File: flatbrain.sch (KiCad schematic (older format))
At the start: 107 parts, among them J1 OLED, SW41 Rotary_Encoder_Switch, SW42 Rotary_Encoder_Switch, U1 Elite-C

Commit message: wip: switches placed, matrix change
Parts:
- removed D1, D12, D13, D24, D25, D36, D37, D46: D_Small, Keebio-Parts:Diode-Hybrid-Back, symbol Device:D_Small
- removed JP1, JP2, JP3: Jumper_NO_Small, Jumper:SolderJumper-2_P1.3mm_Open_Pad1.0x1.5mm, symbol Device:Jumper_NO_Small
- removed MX1, MX12, MX13, MX24, MX25, MX36, MX37, MX46: MX-NoLED, parts:mxchoc_1u, symbol MX_Alps_Hybrid:MX-NoLED
- D1: renamed from D2; footprint Keebio-Parts:Diode-Hybrid-Back -> Keebio-Parts:Diode-dual
- D10: renamed from D11; footprint Keebio-Parts:Diode-Hybrid-Back -> Keebio-Parts:Diode-dual
- D11: renamed from D14; footprint Keebio-Parts:Diode-Hybrid-Back -> Keebio-Parts:Diode-dual
- D12: renamed from D15; footprint Keebio-Parts:Diode-Hybrid-Back -> Keebio-Parts:Diode-dual
- D13: renamed from D16; footprint Keebio-Parts:Diode-Hybrid-Back -> Keebio-Parts:Diode-dual
- D14: renamed from D17; footprint Keebio-Parts:Diode-Hybrid-Back -> Keebio-Parts:Diode-dual
- D15: renamed from D18; footprint Keebio-Parts:Diode-Hybrid-Back -> Keebio-Parts:Diode-dual
- D16: renamed from D19; footprint Keebio-Parts:Diode-Hybrid-Back -> Keebio-Parts:Diode-dual
- D17: renamed from D20; footprint Keebio-Parts:Diode-Hybrid-Back -> Keebio-Parts:Diode-dual
- D18: renamed from D21; footprint Keebio-Parts:Diode-Hybrid-Back -> Keebio-Parts:Diode-dual
- D19: renamed from D22; footprint Keebio-Parts:Diode-Hybrid-Back -> Keebio-Parts:Diode-dual
- D2: renamed from D3; footprint Keebio-Parts:Diode-Hybrid-Back -> Keebio-Parts:Diode-dual
- D20: renamed from D23; footprint Keebio-Parts:Diode-Hybrid-Back -> Keebio-Parts:Diode-dual
- D21: renamed from D26; footprint Keebio-Parts:Diode-Hybrid-Back -> Keebio-Parts:Diode-dual
- D22: renamed from D27; footprint Keebio-Parts:Diode-Hybrid-Back -> Keebio-Parts:Diode-dual
- D23: renamed from D28; footprint Keebio-Parts:Diode-Hybrid-Back -> Keebio-Parts:Diode-dual
- D24: renamed from D29; footprint Keebio-Parts:Diode-Hybrid-Back -> Keebio-Parts:Diode-dual
- D25: renamed from D30; footprint Keebio-Parts:Diode-Hybrid-Back -> Keebio-Parts:Diode-dual
- D26: renamed from D31; footprint Keebio-Parts:Diode-Hybrid-Back -> Keebio-Parts:Diode-dual
- D27: renamed from D32; footprint Keebio-Parts:Diode-Hybrid-Back -> Keebio-Parts:Diode-dual
- D28: renamed from D33; footprint Keebio-Parts:Diode-Hybrid-Back -> Keebio-Parts:Diode-dual
- D29: renamed from D34; footprint Keebio-Parts:Diode-Hybrid-Back -> Keebio-Parts:Diode-dual
- D3: renamed from D4; footprint Keebio-Parts:Diode-Hybrid-Back -> Keebio-Parts:Diode-dual
- D30: renamed from D35; footprint Keebio-Parts:Diode-Hybrid-Back -> Keebio-Parts:Diode-dual
- D32: renamed from D38; footprint Keebio-Parts:Diode-Hybrid-Back -> Keebio-Parts:Diode-dual
- D33: renamed from D39; footprint Keebio-Parts:Diode-Hybrid-Back -> Keebio-Parts:Diode-dual
- D34: renamed from D40; footprint Keebio-Parts:Diode-Hybrid-Back -> Keebio-Parts:Diode-dual
- D35: renamed from D41; footprint Keebio-Parts:Diode-Hybrid-Back -> Keebio-Parts:Diode-dual
- D36: renamed from D42; footprint Keebio-Parts:Diode-Hybrid-Back -> Keebio-Parts:Diode-dual
- D37: renamed from D43; footprint Keebio-Parts:Diode-Hybrid-Back -> Keebio-Parts:Diode-dual
- D38: renamed from D44; footprint Keebio-Parts:Diode-Hybrid-Back -> Keebio-Parts:Diode-dual
- D39: renamed from D45; footprint Keebio-Parts:Diode-Hybrid-Back -> Keebio-Parts:Diode-dual
- D4: renamed from D5; footprint Keebio-Parts:Diode-Hybrid-Back -> Keebio-Parts:Diode-dual
- D5: renamed from D6; footprint Keebio-Parts:Diode-Hybrid-Back -> Keebio-Parts:Diode-dual
- D6: renamed from D7; footprint Keebio-Parts:Diode-Hybrid-Back -> Keebio-Parts:Diode-dual
- D7: renamed from D8; footprint Keebio-Parts:Diode-Hybrid-Back -> Keebio-Parts:Diode-dual
- D8: renamed from D9; footprint Keebio-Parts:Diode-Hybrid-Back -> Keebio-Parts:Diode-dual
- D9: renamed from D10; footprint Keebio-Parts:Diode-Hybrid-Back -> Keebio-Parts:Diode-dual
- MX1: renamed from MX2; footprint parts:mxchoc_1u -> parts:mix_1u; symbol MX_Alps_Hybrid:MX-NoLED -> flatbrain:MX_Alps_Hybrid_MX-NoLED
- MX10: renamed from MX11; footprint parts:mxchoc_1u -> parts:mix_1u; symbol MX_Alps_Hybrid:MX-NoLED -> flatbrain:MX_Alps_Hybrid_MX-NoLED
- MX11: renamed from MX14; footprint parts:mxchoc_1u -> parts:mix_1u; symbol MX_Alps_Hybrid:MX-NoLED -> flatbrain:MX_Alps_Hybrid_MX-NoLED
- MX12: renamed from MX15; footprint parts:mxchoc_1u -> parts:mix_1u; symbol MX_Alps_Hybrid:MX-NoLED -> flatbrain:MX_Alps_Hybrid_MX-NoLED
- MX13: renamed from MX16; footprint parts:mxchoc_1u -> parts:mix_1u; symbol MX_Alps_Hybrid:MX-NoLED -> flatbrain:MX_Alps_Hybrid_MX-NoLED
- MX14: renamed from MX17; footprint parts:mxchoc_1u -> parts:mix_1u; symbol MX_Alps_Hybrid:MX-NoLED -> flatbrain:MX_Alps_Hybrid_MX-NoLED
- MX15: renamed from MX18; footprint parts:mxchoc_1u -> parts:mix_1u; symbol MX_Alps_Hybrid:MX-NoLED -> flatbrain:MX_Alps_Hybrid_MX-NoLED
- MX16: renamed from MX19; footprint parts:mxchoc_1u -> parts:mix_1u; symbol MX_Alps_Hybrid:MX-NoLED -> flatbrain:MX_Alps_Hybrid_MX-NoLED
- MX17: renamed from MX20; footprint parts:mxchoc_1u -> parts:mix_1u; symbol MX_Alps_Hybrid:MX-NoLED -> flatbrain:MX_Alps_Hybrid_MX-NoLED
- MX18: renamed from MX21; footprint parts:mxchoc_1u -> parts:mix_1u; symbol MX_Alps_Hybrid:MX-NoLED -> flatbrain:MX_Alps_Hybrid_MX-NoLED
- MX19: renamed from MX22; footprint parts:mxchoc_1u -> parts:mix_1u; symbol MX_Alps_Hybrid:MX-NoLED -> flatbrain:MX_Alps_Hybrid_MX-NoLED
- MX2: renamed from MX3; footprint parts:mxchoc_1u -> parts:mix_1u; symbol MX_Alps_Hybrid:MX-NoLED -> flatbrain:MX_Alps_Hybrid_MX-NoLED
- MX20: renamed from MX23; footprint parts:mxchoc_1u -> parts:mix_1u; symbol MX_Alps_Hybrid:MX-NoLED -> flatbrain:MX_Alps_Hybrid_MX-NoLED
- MX21: renamed from MX26; footprint parts:mxchoc_1u -> parts:mix_1u; symbol MX_Alps_Hybrid:MX-NoLED -> flatbrain:MX_Alps_Hybrid_MX-NoLED
- MX22: renamed from MX27; footprint parts:mxchoc_1u -> parts:mix_1u; symbol MX_Alps_Hybrid:MX-NoLED -> flatbrain:MX_Alps_Hybrid_MX-NoLED
- MX23: renamed from MX28; footprint parts:mxchoc_1u -> parts:mix_1u; symbol MX_Alps_Hybrid:MX-NoLED -> flatbrain:MX_Alps_Hybrid_MX-NoLED
- MX24: renamed from MX29; footprint parts:mxchoc_1u -> parts:mix_1u; symbol MX_Alps_Hybrid:MX-NoLED -> flatbrain:MX_Alps_Hybrid_MX-NoLED
- MX25: renamed from MX30; footprint parts:mxchoc_1u -> parts:mix_1u; symbol MX_Alps_Hybrid:MX-NoLED -> flatbrain:MX_Alps_Hybrid_MX-NoLED
- MX26: renamed from MX31; footprint parts:mxchoc_1u -> parts:mix_1u; symbol MX_Alps_Hybrid:MX-NoLED -> flatbrain:MX_Alps_Hybrid_MX-NoLED
- MX27: renamed from MX32; footprint parts:mxchoc_1u -> parts:mix_1u; symbol MX_Alps_Hybrid:MX-NoLED -> flatbrain:MX_Alps_Hybrid_MX-NoLED
- MX28: renamed from MX33; footprint parts:mxchoc_1u -> parts:mix_1u; symbol MX_Alps_Hybrid:MX-NoLED -> flatbrain:MX_Alps_Hybrid_MX-NoLED
- MX29: renamed from MX34; footprint parts:mxchoc_1u -> parts:mix_1u; symbol MX_Alps_Hybrid:MX-NoLED -> flatbrain:MX_Alps_Hybrid_MX-NoLED
- MX3: renamed from MX4; footprint parts:mxchoc_1u -> parts:mix_1u; symbol MX_Alps_Hybrid:MX-NoLED -> flatbrain:MX_Alps_Hybrid_MX-NoLED
- MX30: renamed from MX35; footprint parts:mxchoc_1u -> parts:mix_1u; symbol MX_Alps_Hybrid:MX-NoLED -> flatbrain:MX_Alps_Hybrid_MX-NoLED
- MX32: renamed from MX38; footprint parts:mxchoc_1u -> parts:mix_1u; symbol MX_Alps_Hybrid:MX-NoLED -> flatbrain:MX_Alps_Hybrid_MX-NoLED
- MX33: renamed from MX39; footprint parts:mxchoc_1u -> parts:mix_1u; symbol MX_Alps_Hybrid:MX-NoLED -> flatbrain:MX_Alps_Hybrid_MX-NoLED
- MX34: renamed from MX40; footprint parts:mxchoc_1u -> parts:mix_1u; symbol MX_Alps_Hybrid:MX-NoLED -> flatbrain:MX_Alps_Hybrid_MX-NoLED
- MX37: renamed from MX43; footprint parts:mxchoc_1u -> parts:mix_1u; symbol MX_Alps_Hybrid:MX-NoLED -> flatbrain:MX_Alps_Hybrid_MX-NoLED
- MX38: renamed from MX44; footprint parts:mxchoc_1u -> parts:mix_1u; symbol MX_Alps_Hybrid:MX-NoLED -> flatbrain:MX_Alps_Hybrid_MX-NoLED
- MX39: renamed from MX45; footprint parts:mxchoc_1u -> parts:mix_1u; symbol MX_Alps_Hybrid:MX-NoLED -> flatbrain:MX_Alps_Hybrid_MX-NoLED
- MX4: renamed from MX5; footprint parts:mxchoc_1u -> parts:mix_1u; symbol MX_Alps_Hybrid:MX-NoLED -> flatbrain:MX_Alps_Hybrid_MX-NoLED
- MX5: renamed from MX6; footprint parts:mxchoc_1u -> parts:mix_1u; symbol MX_Alps_Hybrid:MX-NoLED -> flatbrain:MX_Alps_Hybrid_MX-NoLED
- MX6: renamed from MX7; footprint parts:mxchoc_1u -> parts:mix_1u; symbol MX_Alps_Hybrid:MX-NoLED -> flatbrain:MX_Alps_Hybrid_MX-NoLED
- MX7: renamed from MX8; footprint parts:mxchoc_1u -> parts:mix_1u; symbol MX_Alps_Hybrid:MX-NoLED -> flatbrain:MX_Alps_Hybrid_MX-NoLED
- MX8: renamed from MX9; footprint parts:mxchoc_1u -> parts:mix_1u; symbol MX_Alps_Hybrid:MX-NoLED -> flatbrain:MX_Alps_Hybrid_MX-NoLED
- MX9: renamed from MX10; footprint parts:mxchoc_1u -> parts:mix_1u; symbol MX_Alps_Hybrid:MX-NoLED -> flatbrain:MX_Alps_Hybrid_MX-NoLED
- renumbered SW41 to SW1, SW42 to SW2
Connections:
- net labels removed: COL10, COL11
- wire segments 168 -> 141
- no-connect marks 3 -> 4

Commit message: update schema
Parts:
- removed D36: D_Small, Keebio-Parts:Diode-dual, symbol Device:D_Small
- removed SW2: Rotary_Encoder_Switch, parts:rotary_x_mxchoc, symbol Device:Rotary_Encoder_Switch
- added J2: Conn_01x05, Kicad-Footprints:pimoroni_trackball, symbol Connector_Generic:Conn_01x05
- SW1: footprint parts:rotary_x_mxchoc -> parts:rotary_x_mx
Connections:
- net GND: now also J2.5 (Pin_5)
- net SCL: now also J2.3 (Pin_3)
- net SDA: now also J2.2 (Pin_2)
- net VCC: now also J2.1 (Pin_1)
- no-connect marks 4 -> 5
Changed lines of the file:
@@
 NoConn ~ 1000 5950
-$Comp
-L Device:Rotary_Encoder_Switch SW2
-U 1 1 5EE87CC0
-P 8150 4150
-F 0 "SW2" H 8150 3900 50  0000 C CNN
-F 1 "Rotary_Encoder_Switch" H 8150 3800 50  0000 C CNN
-F 2 "parts:rotary_x_mxchoc" H 8000 4310 50  0001 C CNN
-F 3 "~" H 8150 4410 50  0001 C CNN
-	1    8150 4150
-	0    -1   -1   0
-$EndComp
 $Comp
 L Device:Rotary_Encoder_Switch SW1
@@
 F 0 "SW1" H 7600 4517 50  0000 C CNN
 F 1 "Rotary_Encoder_Switch" H 7600 4426 50  0000 C CNN
-F 2 "parts:rotary_x_mxchoc" H 7450 4310 50  0001 C CNN
+F 2 "parts:rotary_x_mx" H 7450 4310 50  0001 C CNN
 F 3 "~" H 7600 4410 50  0001 C CNN
 	1    7600 4150
@@
 	6800 3650 7500 3650
 $Comp
-L Device:D_Small D36
-U 1 1 5F0CAFA9
-P 8050 3750
-F 0 "D36" V 8096 3680 50  0000 R CNN
-F 1 "D_Small" V 8005 3680 50  0000 R CNN
-F 2 "Keebio-Parts:Diode-dual" V 8050 3750 50  0001 C CNN
-F 3 "~" V 8050 3750 50  0001 C CNN
-	1    8050 3750
-	0    1    1    0
-$EndComp
-Connection ~ 8050 3650
-Wire Wire Line
-	8050 3650 8450 3650
-$Comp
 L Device:D_Small D35
 U 1 1 5F0CB401
@@
 $EndComp
 Connection ~ 7500 3650
-Wire Wire Line
-	7500 3650 8050 3650
 Connection ~ 7700 2600
-Wire Wire Line
-	8250 3850 8250 2600
-Connection ~ 8250 2600
 Wire Wire Line
 	7700 2600 7700 3850
@@
 Text GLabel 7700 4450 3    50   Input ~ 0
 ENC1B
-Text GLabel 8050 4450 3    50   Input ~ 0
-ENC2A
-Text GLabel 8250 4450 3    50   Input ~ 0
-ENC2B
 $Comp
 L power:GND #PWR07
@@
 F 3 "" H 7600 4450 50  0001 C CNN
 	1    7600 4450
-	1    0    0    -1
-$EndComp
-$Comp
-L power:GND #PWR08
-U 1 1 5F0FFEF3
-P 8150 4450
-F 0 "#PWR08" H 8150 4200 50  0001 C CNN
-F 1 "GND" H 8155 4277 50  0000 C CNN
-F 2 "" H 8150 4450 50  0001 C CNN
-F 3 "" H 8150 4450 50  0001 C CNN
-	1    8150 4450
 	1    0    0    -1
 $EndComp
@@
 Wire Wire Line
 	4900 3650 5700 3650
+$Comp
+L Connector_Generic:Conn_01x05 J2
+U 1 1 5FFEA824
+P 6600 4850
+F 0 "J2" H 6680 4892 50  0000 L CNN
+F 1 "Conn_01x05" H 6680 4801 50  0000 L CNN
+F 2 "Kicad-Footprints:pimoroni_trackball" H 6600 4850 50  0001 C CNN
+F 3 "~" H 6600 4850 50  0001 C CNN
+	1    6600 4850
+	1    0    0    -1
+$EndComp
+$Comp
+L power:VCC #PWR0101
+U 1 1 5FFF95B2
+P 6400 4650
+F 0 "#PWR0101" H 6400 4500 50  0001 C CNN
+F 1 "VCC" V 6415 4778 50  0000 L CNN
+F 2 "" H 6400 4650 50  0001 C CNN
+F 3 "" H 6400 4650 50  0001 C CNN
+	1    6400 4650
+	0    -1   -1   0
+$EndComp
+Text GLabel 6400 4750 0    50   Input ~ 0
+SDA
+Text GLabel 6400 4850 0    50   Input ~ 0
+SCL
+NoConn ~ 6400 4950
+$Comp
+L power:GND #PWR0102
+U 1 1 60019A0F
+P 6400 5050
+F 0 "#PWR0102" H 6400 4800 50  0001 C CNN
+F 1 "GND" V 6405 4922 50  0000 R CNN
+F 2 "" H 6400 5050 50  0001 C CNN
+F 3 "" H 6400 5050 50  0001 C CNN
+	1    6400 5050
+	0    1    1    0
+$EndComp
+Wire Wire Line
+	7500 3650 8450 3650
 $EndSCHEMATC

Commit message: all route done
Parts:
- D1, D10, D11, D12, D13, D14, D15, D16, D17, D18, D19, D2, D20, D21, D22, D23, D24, D25, D26, D27, D28, D29, D3, D30, D32, D33, D34, D35, D37, D38, D39, D4, D5, D6, D7, D8, D9: footprint Keebio-Parts:Diode-dual -> Keebio-Parts:Diode-Hybrid-Back
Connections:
- net COL0: now also U1.20 (F4); no longer U1.18 (F6)
- net COL1: now also U1.19 (F5); no longer U1.17 (F7)
- net COL2: now also U1.18 (F6); no longer U1.16 (B1)
- net COL3: now also U1.17 (F7); no longer U1.15 (B3)
- net COL4: now also U1.16 (B1); no longer U1.14 (B2)
- net COL5: now also U1.10 (E6); no longer U1.13 (B6)
- net COL6: now also U1.9 (D7); no longer U1.12 (B5)
- net COL7: now also U1.8 (C6); no longer U1.11 (B4)
- net COL8: now also U1.7 (D4); no longer U1.10 (E6)
- net COL9: now also U1.2 (D2); no longer U1.9 (D7)
- net ROW0: now also U1.15 (B3); no longer U1.7 (D4)
- net ROW1: now also U1.14 (B2); no longer U1.2 (D2)
- net ROW2: now also U1.11 (B4); no longer U1.20 (F4)
- net ROW3: now also U1.12 (B5); no longer U1.19 (F5)
- net ENC1A renamed ENCA
- net ENC1B renamed ENCB
- net ENC2A: no longer names the net of U1.25 (B7)
- net ENC2B: no longer names the net of U1.26 (D5)
- no-connect marks 5 -> 7
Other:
- moved on the sheet: J2

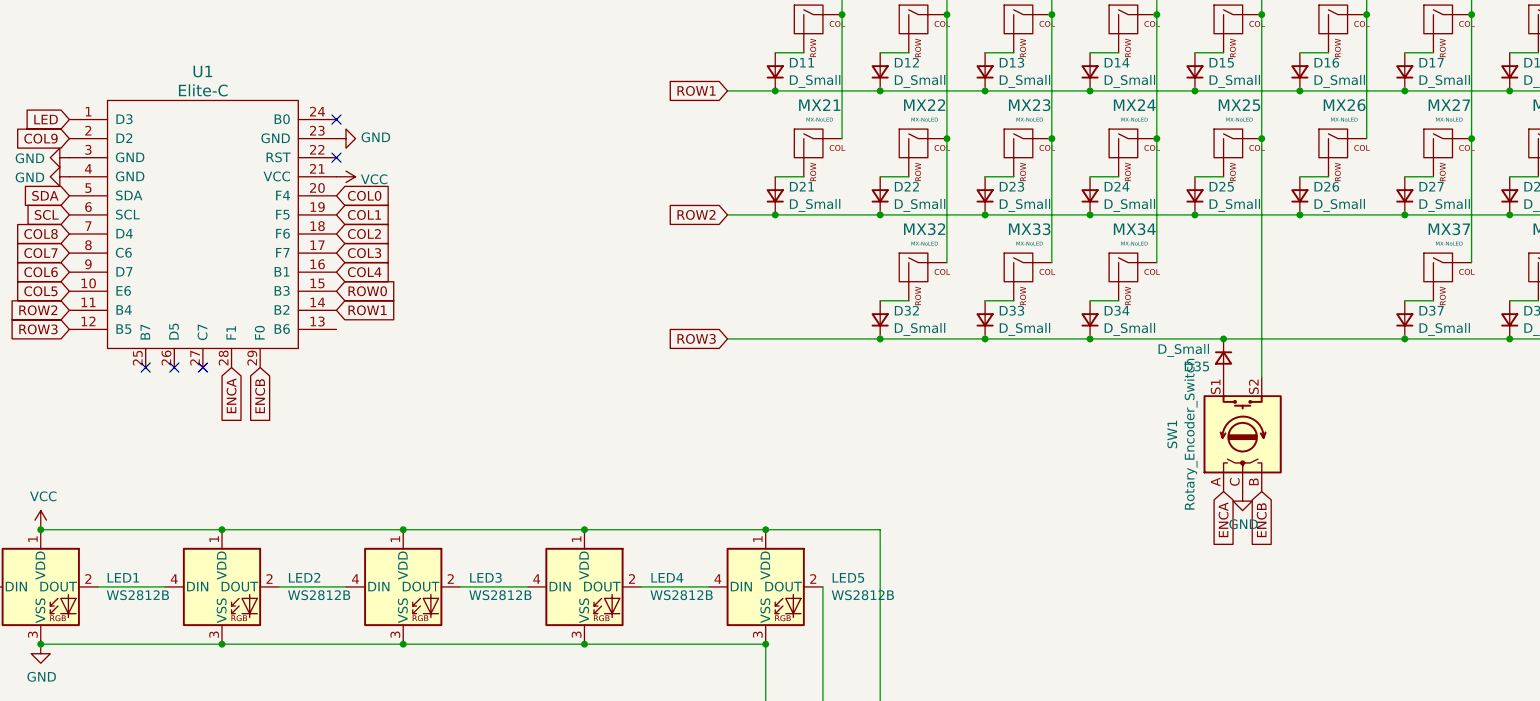
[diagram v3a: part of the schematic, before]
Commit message: rev3 is done
add a rotary
add silk
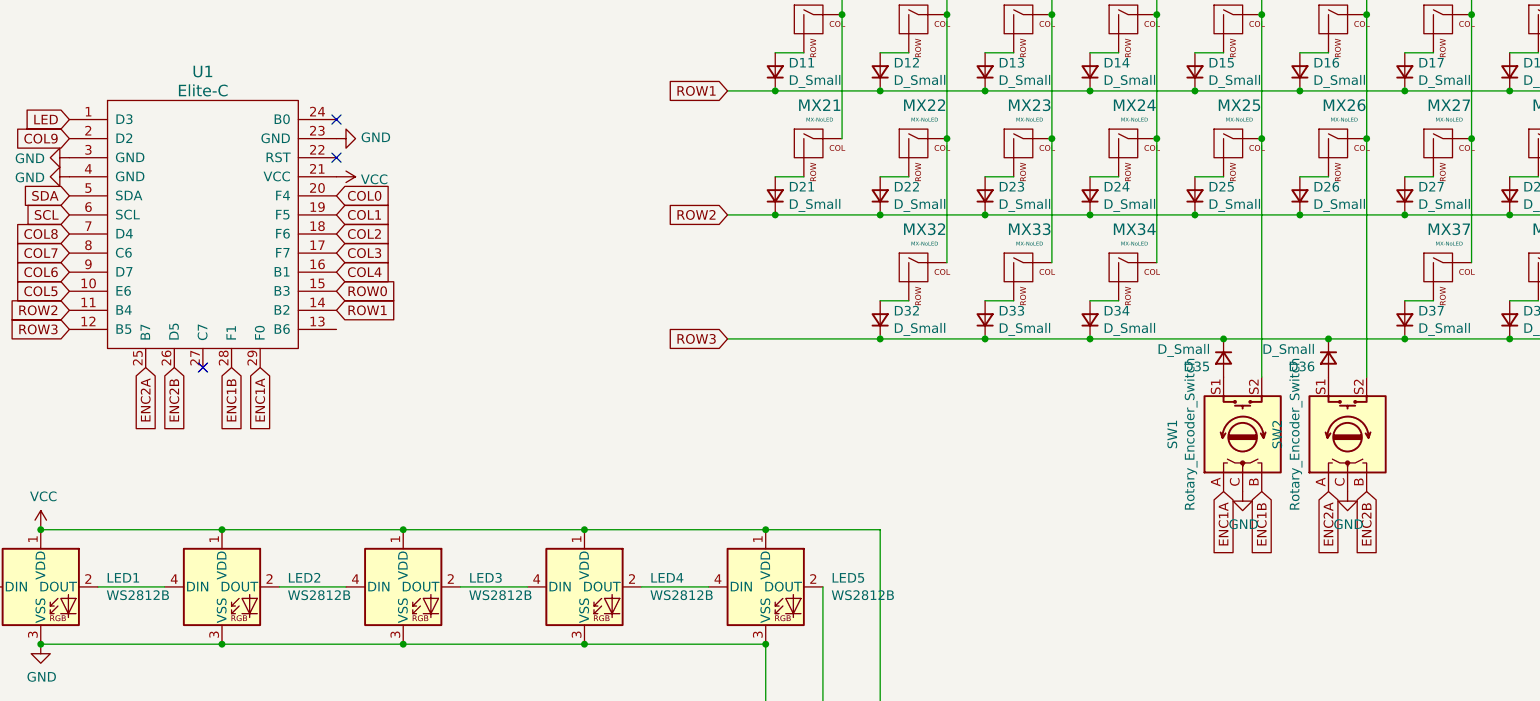
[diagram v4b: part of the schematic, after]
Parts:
- added D36: D_Small, Keebio-Parts:Diode-Hybrid-Back, symbol Device:D_Small
- added SW2: Rotary_Encoder_Switch, parts:rotary_full, symbol Device:Rotary_Encoder_Switch
- SW1: footprint parts:rotary_x_mx -> parts:rotary_full
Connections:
- net COL5: now also SW2.S2
- net GND: now also SW2.C
- net ROW3: now also D36.1 (K)
- net ENC2A: now reaches U1.25 (B7)
- net ENC2A: now also SW2.A
- net ENC2B: now reaches U1.26 (D5)
- net ENC2B: now also SW2.B
- net ENCA renamed ENC1A
- net ENC1A: now also U1.29 (F0); no longer U1.28 (F1)
- net ENCB renamed ENC1B
- net ENC1B: now also U1.28 (F1); no longer U1.29 (F0)
- new net: D36.2 (A), SW2.S1
- no-connect marks 7 -> 5
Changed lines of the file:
@@
 F 0 "SW1" H 7600 4517 50  0000 C CNN
 F 1 "Rotary_Encoder_Switch" H 7600 4426 50  0000 C CNN
-F 2 "parts:rotary_x_mx" H 7450 4310 50  0001 C CNN
+F 2 "parts:rotary_full" H 7450 4310 50  0001 C CNN
 F 3 "~" H 7600 4410 50  0001 C CNN
 	1    7600 4150
@@
 Wire Wire Line
 	7700 2600 7700 3850
-Text GLabel 7500 4450 3    50   Input ~ 0
-ENCA
-Text GLabel 7700 4450 3    50   Input ~ 0
-ENCB
 $Comp
 L power:GND #PWR07
@@
 Text GLabel 2850 3500 2    50   Input ~ 0
 ROW1
+Text GLabel 2450 3800 3    50   Input ~ 0
+ENC1A
 Text GLabel 2300 3800 3    50   Input ~ 0
-ENCA
-Text GLabel 2450 3800 3    50   Input ~ 0
-ENCB
+ENC1B
 NoConn ~ 2150 3800
 NoConn ~ 2850 2700
@@
 	0    -1   -1   0
 $EndComp
-Wire Wire Line
-	7500 3650 8450 3650
-NoConn ~ 1850 3800
-NoConn ~ 2000 3800
+$Comp
+L Device:D_Small D36
+U 1 1 600D8C59
+P 8050 3750
+F 0 "D36" V 8096 3680 50  0000 R CNN
+F 1 "D_Small" V 8005 3680 50  0000 R CNN
+F 2 "Keebio-Parts:Diode-Hybrid-Back" V 8050 3750 50  0001 C CNN
+F 3 "~" V 8050 3750 50  0001 C CNN
+	1    8050 3750
+	0    1    1    0
+$EndComp
+$Comp
+L power:GND #PWR0103
+U 1 1 600D8C62
+P 8150 4450
+F 0 "#PWR0103" H 8150 4200 50  0001 C CNN
+F 1 "GND" H 8155 4277 50  0000 C CNN
+F 2 "" H 8150 4450 50  0001 C CNN
+F 3 "" H 8150 4450 50  0001 C CNN
+	1    8150 4450
+	1    0    0    -1
+$EndComp
+$Comp
+L Device:Rotary_Encoder_Switch SW2
+U 1 1 600D8C53
+P 8150 4150
+F 0 "SW2" H 8150 4517 50  0000 C CNN
+F 1 "Rotary_Encoder_Switch" H 8150 4426 50  0000 C CNN
+F 2 "parts:rotary_full" H 8000 4310 50  0001 C CNN
+F 3 "~" H 8150 4410 50  0001 C CNN
+	1    8150 4150
+	0    -1   -1   0
+$EndComp
+Connection ~ 8050 3650
+Wire Wire Line
+	8050 3650 8450 3650
+Wire Wire Line
+	7500 3650 8050 3650
+Wire Wire Line
+	8250 3850 8250 2600
+Connection ~ 8250 2600
+Text GLabel 1850 3800 3    50   Input ~ 0
+ENC2A
+Text GLabel 2000 3800 3    50   Input ~ 0
+ENC2B
+Text GLabel 7500 4450 3    50   Input ~ 0
+ENC1A
+Text GLabel 7700 4450 3    50   Input ~ 0
+ENC1B
+Text GLabel 8050 4450 3    50   Input ~ 0
+ENC2A
+Text GLabel 8250 4450 3    50   Input ~ 0
+ENC2B
 $EndSCHEMATC

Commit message: half pcba
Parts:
- removed U1: Elite-C, Keebio-Parts:Elite-C, symbol flatbrain:Elite-C
- added C1: 1uF, Capacitor_SMD:C_0805_2012Metric, symbol Device:C_Small
- added C2, C3, C4, C8: 0.1uF, Capacitor_SMD:C_0805_2012Metric, symbol Device:C_Small
- added C5: 10uF, Capacitor_SMD:C_0805_2012Metric, symbol Device:C_Small
- added C6, C7: 22pF, Capacitor_SMD:C_0805_2012Metric, symbol Device:C_Small
- added F1: 500mA, Fuse:Fuse_1206_3216Metric, symbol Device:Polyfuse_Small
- added FB1: Ferrite_Bead_Small, Inductor_SMD:L_0805_2012Metric_Pad1.15x1.40mm_HandSolder, symbol Device:Ferrite_Bead_Small
- added J3: AVR-ISP-6, random-keyboard-parts:Reset_Pretty-Mask, symbol Connector:AVR-ISP-6
- added R1, R4: 10k, Resistor_SMD:R_0805_2012Metric, symbol Device:R_Small
- added R2, R3: 22, Resistor_SMD:R_0805_2012Metric, symbol Device:R_Small
- added R5, R6: 5.1k, Resistor_SMD:R_0805_2012Metric, symbol Device:R_Small
- added SW3: SW_Push, random-keyboard-parts:SKQG-1155865, symbol Switch:SW_Push
- added U1: ATmega32U4-AU, Package_QFP:TQFP-44_10x10mm_P0.8mm, symbol MCU_Microchip_ATmega:ATmega32U4-AU
- added U2: PRTR5V0U2X, random-keyboard-parts:SOT143B, symbol Power_Protection:PRTR5V0U2X
- added USB1: USB_C_Receptacle_USB2.0, Connector_USB:USB_C_Receptacle_HRO_TYPE-C-31-M-12, symbol Connector:USB_C_Receptacle_USB2.0
- added Y1: 16MHz, Crystal:Crystal_SMD_3225-4Pin_3.2x2.5mm, symbol Device:Crystal_GND24_Small
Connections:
- net COL0: now also U1.8 (PB0)
- net COL1: now also J3.3 (SCK), U1.9 (PB1)
- net COL2: now also J3.4 (MOSI), U1.10 (PB2)
- net COL3: now also J3.1 (MISO), U1.11 (PB3)
- net COL4: now also U1.12 (PB7)
- net COL5: now also U1.20 (PD2)
- net COL6: now also U1.29 (PB5)
- net COL7: now also U1.25 (PD4)
- net COL8: now also U1.39 (PF4)
- net COL9: now also U1.38 (PF5)
- net ENC1A: now also U1.21 (PD3)
- net ENC1B: now also U1.22 (PD5)
- net ENC2A: now also U1.32 (PC7)
- net ENC2B: now also U1.31 (PC6)
- net GND: now also C1.2, C2.2, C3.2, C4.2, C5.2, C6.2, C7.2, C8.2, FB1.1, J3.6 (GND), R1.1, R5.1, R6.1, SW3.1, U1.15 (GND), U1.23 (GND), U1.35 (GND), U1.43 (GND), U1.5 (UGND), U2.1 (GND), USB1.A1 (GND), USB1.A12 (GND), USB1.B1 (GND), USB1.B12 (GND), Y1.2, Y1.4
- net LED: now also U1.1 (PE6)
- net ROW0: now also U1.28 (PB4)
- net ROW1: now also U1.30 (PB6)
- net ROW2: now also U1.27 (PD7)
- net ROW3: now also U1.26 (PD6)
- net SCL: now also U1.18 (PD0)
- net SDA: now also U1.19 (PD1)
- net VCC: now also F1.2, U2.4 (VCC), USB1.A4 (VBUS), USB1.A9 (VBUS), USB1.B4 (VBUS), USB1.B9 (VBUS); no longer J1.3 (Pin_3), J2.1 (Pin_1), LED1.1 (VDD), LED10.1 (VDD), LED2.1 (VDD), LED3.1 (VDD), LED4.1 (VDD), LED5.1 (VDD), LED6.1 (VDD), LED7.1 (VDD), LED8.1 (VDD), LED9.1 (VDD)
- new net: R1.2, U1.33 (~HWB~/PE2)
- new net: C1.1, U1.6 (UCAP)
- new net: R5.2, USB1.A5 (CC1)
- new net: R6.2, USB1.B5 (CC2)
- new net +5V: C2.1, C3.1, C4.1, C5.1, C8.1, F1.1, J1.3 (Pin_3), J2.1 (Pin_1), J3.2 (VCC), LED1.1 (VDD), LED10.1 (VDD), LED2.1 (VDD), LED3.1 (VDD), LED4.1 (VDD), LED5.1 (VDD), LED6.1 (VDD), LED7.1 (VDD), LED8.1 (VDD), LED9.1 (VDD), R4.1, U1.14 (VCC), U1.2 (UVCC), U1.24 (AVCC), U1.34 (VCC), U1.44 (AVCC), U1.7 (VBUS)
- new net D+: R3.1, U1.4 (D+)
- new net D-: R2.1, U1.3 (D-)
- new net DN: R2.2, U2.3 (I/O2), USB1.A7 (D-), USB1.B7 (D-)
- new net DP: R3.2, U2.2 (I/O1), USB1.A6 (D+), USB1.B6 (D+)
- new net Earth: FB1.2, USB1.S1 (SHIELD)
- new net RST: J3.5 (~RST), R4.2, SW3.2, U1.13 (~RESET)
- new net XTAL1: C6.1, U1.17 (XTAL1), Y1.1
- new net XTAL2: C7.1, U1.16 (XTAL2), Y1.3
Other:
- moved on the sheet: D1, D10, D11, D12, D13, D14, D15, D16, D17, D18, D19, D2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

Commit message: pcba over
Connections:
- net COL5: now also U1.37 (PF6); no longer U1.20 (PD2)
- net COL6: now also U1.38 (PF5); no longer U1.29 (PB5)
- net COL7: now also U1.39 (PF4); no longer U1.25 (PD4)
- net COL8: now also U1.40 (PF1); no longer U1.39 (PF4)
- net COL9: now also U1.41 (PF0); no longer U1.38 (PF5)
- net ROW1: now also U1.27 (PD7); no longer U1.30 (PB6)
- net ROW2: now also U1.30 (PB6); no longer U1.27 (PD7)
- net ROW3: now also U1.29 (PB5); no longer U1.26 (PD6)
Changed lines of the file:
@@
 Text GLabel 2750 1400 3    50   Input ~ 0
 COL3
-Text GLabel 2400 2650 2    50   Input ~ 0
+Text GLabel 2400 3650 2    50   Input ~ 0
 COL7
-Text GLabel 2400 2950 2    50   Input ~ 0
+Text GLabel 2400 1650 2    50   Input ~ 0
 ROW2
 $Comp
@@
 Wire Wire Line
 	9400 3150 9400 2500
-Text GLabel 2400 2850 2    50   Input ~ 0
+Text GLabel 2400 1550 2    50   Input ~ 0
 ROW3
-Text GLabel 2400 1550 2    50   Input ~ 0
+Text GLabel 2400 3750 2    50   Input ~ 0
 COL6
 $Comp
@@
 Text GLabel 2400 1750 2    50   Input ~ 0
 COL4
-Text GLabel 2400 2450 2    50   Input ~ 0
+Text GLabel 2400 3850 2    50   Input ~ 0
 COL5
-Text GLabel 2400 3650 2    50   Input ~ 0
+Text GLabel 2400 3550 2    50   Input ~ 0
 COL8
-Text GLabel 2400 3750 2    50   Input ~ 0
+Text GLabel 2400 3450 2    50   Input ~ 0
 COL9
-Text GLabel 2400 1650 2    50   Input ~ 0
+Text GLabel 2400 2950 2    50   Input ~ 0
 ROW1
 Text GLabel 2400 2550 2    50   Input ~ 0

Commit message: ready to prod
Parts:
- renumbered SW3 to RST1
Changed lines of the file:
@@
 RST
 $Comp
-L Switch:SW_Push SW3
+L Switch:SW_Push RST1
 U 1 1 60A0107B
 P 4750 5000
-F 0 "SW3" H 4750 5285 50  0000 C CNN
+F 0 "RST1" H 4750 5285 50  0000 C CNN
 F 1 "SW_Push" H 4750 5194 50  0000 C CNN
 F 2 "random-keyboard-parts:SKQG-1155865" H 4750 5200 50  0001 C CNN
